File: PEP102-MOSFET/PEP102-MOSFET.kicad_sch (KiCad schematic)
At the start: 23 parts, among them J1 Screw_Terminal_01x02, J2 Screw_Terminal_01x02, J3 Screw_Terminal_01x02, J4 Screw_Terminal_01x02, J5 Screw_Terminal_01x02, Q13 AO3400A, Q8 AO3401A

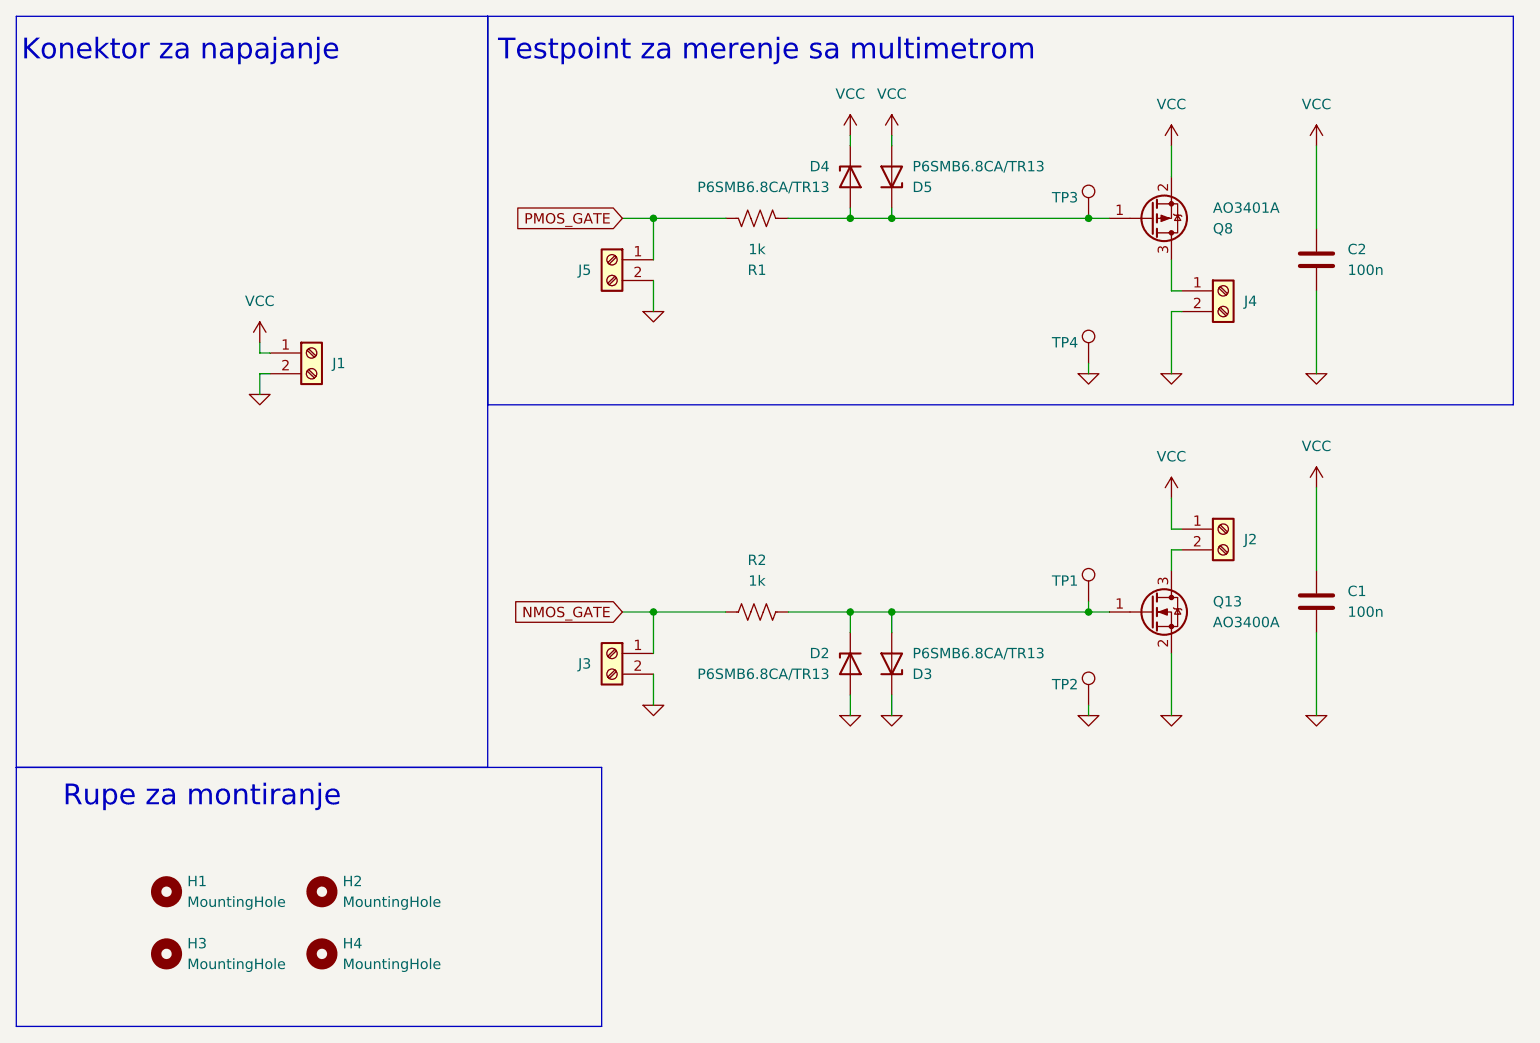
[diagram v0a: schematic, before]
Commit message: Uklonjen PMOS sa PEP102 jer nema prostora.
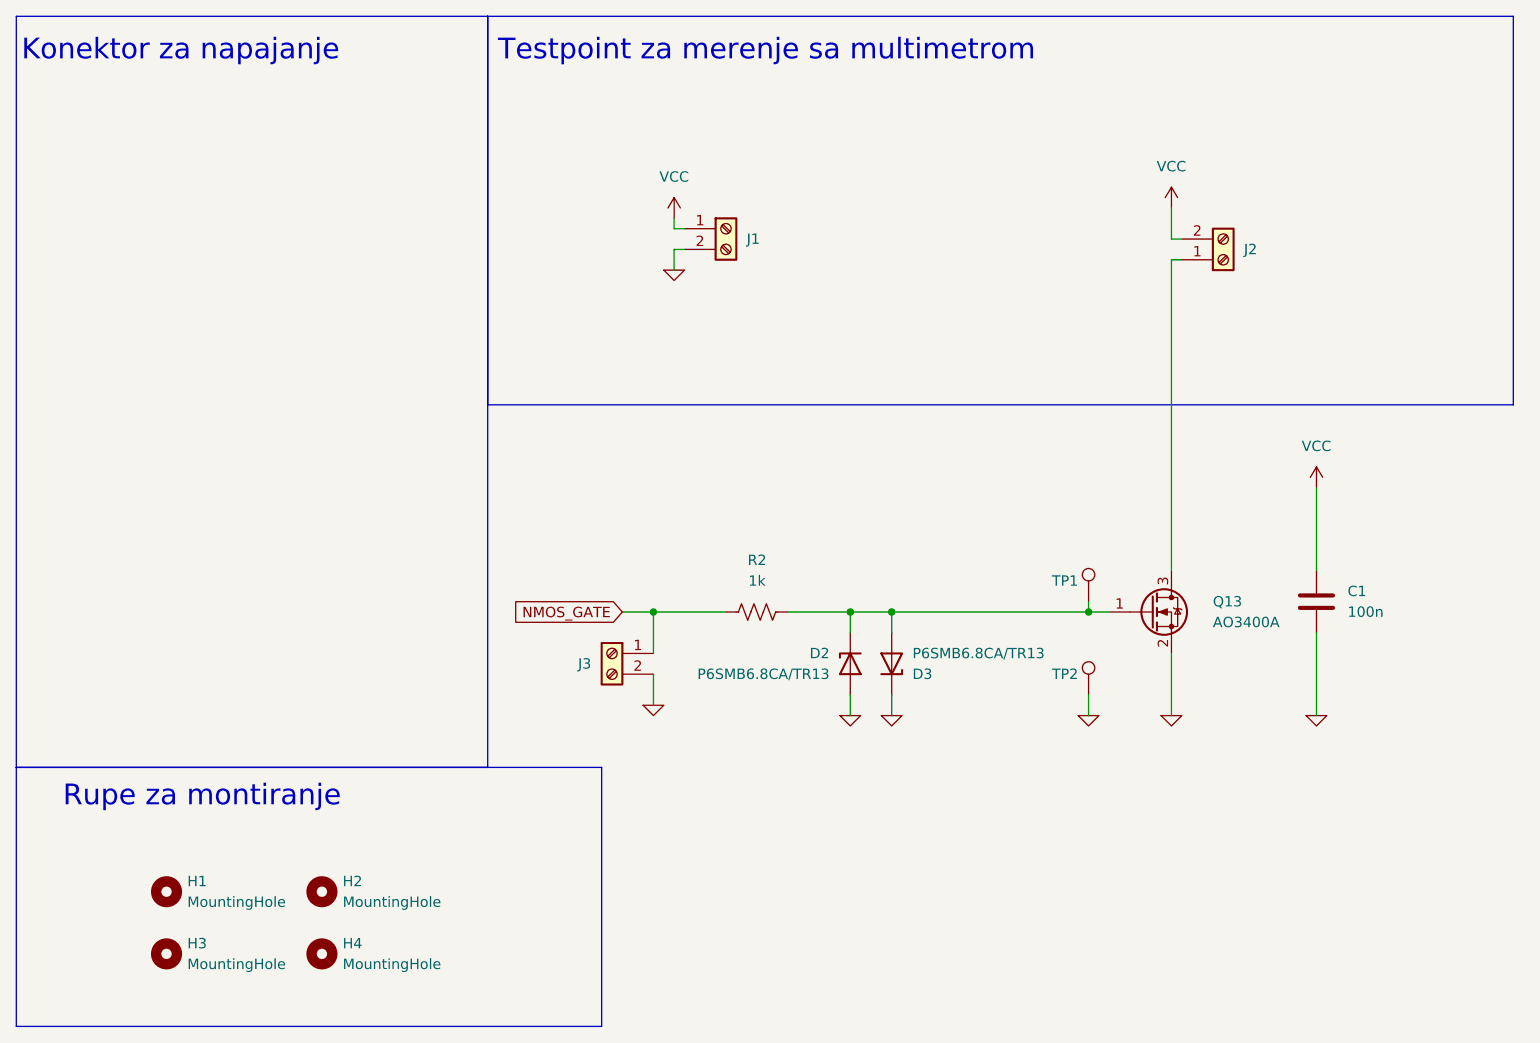
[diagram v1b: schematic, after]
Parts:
- removed C2: 100n, Capacitor_SMD:C_1206_3216Metric_Pad1.33x1.80mm_HandSolder, symbol Device:C
- removed D4, D5: P6SMB6.8CA/TR13, Diode_SMD:D_SMB_Handsoldering, symbol Device:D_Zener
- removed J4, J5: Screw_Terminal_01x02, PEP_library:TerminalBlock_Phoenix_MKDS-1,5-2-5.08_1x02_P5.08mm_Horizontal, symbol PEP_library:Screw_Terminal_01x02
- removed Q8: AO3401A, Package_TO_SOT_SMD:SOT-23, symbol Transistor_FET:AO3401A
- removed R1: 1k, Resistor_SMD:R_1206_3216Metric_Pad1.30x1.75mm_HandSolder, symbol Device:R_US
- removed TP3, TP4: TestPoint, symbol Connector:TestPoint
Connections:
- net VCC: now also J2.2 (Pin_2); no longer J2.1 (Pin_1)
- net at Q13.3 (D): now also J2.1 (Pin_1); no longer J2.2 (Pin_2)
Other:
- moved on the sheet: J1, J2, TP2

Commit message: Placement done.
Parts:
- removed D2, D3: P6SMB6.8CA/TR13, Diode_SMD:D_SMB_Handsoldering, symbol Device:D_Zener
- removed Q13: AO3400A, Package_TO_SOT_SMD:SOT-23, symbol Transistor_FET:AO3400A
- added D14: PSM712-LF-T7, Package_TO_SOT_SMD:SOT-23, symbol Device:D_Zener_Dual_CommonAnode_KKA
- added Q19: 2N7002, Package_TO_SOT_SMD:SOT-23, symbol Transistor_FET:AO3400A
- added TP3: TestPoint, TestPoint:TestPoint_Pad_D4.0mm, symbol Connector:TestPoint
- TP1, TP2: footprint (none) -> TestPoint:TestPoint_Pad_D4.0mm
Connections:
- net 0: now also D14.3 (A), Q19.2 (S)
- net VCC: now also J2.1 (Pin_1); no longer J2.2 (Pin_2)
- net at R2.2, TP1.1: now also D14.1 (K), D14.2 (K), Q19.1 (G)
- new net: J2.2 (Pin_2), Q19.3 (D), TP3.1

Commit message: Done, kinda
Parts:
- J2: footprint PEP_library:TerminalBlock_Phoenix_MKDS-1,5-2-5.08_1x02_P5.08mm_Horizontal -> PEP_library:Screw terminal
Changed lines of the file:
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@@
 			)
 		)
-		(property "Footprint" "PEP_library:TerminalBlock_Phoenix_MKDS-1,5-2-5.08_1x02_P5.08mm_Horizontal"
+		(property "Footprint" "PEP_library:Screw terminal"
 			(at 160.02 39.37 0)
 			(effects

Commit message: Done, kinda
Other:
- note added: "MOSFET"
- note added: "Zaštita gate-a"
- note removed: "Testpoint za merenje sa multimetrom"
- moved on the sheet: C1, D14, J1, J2, J3, Q19, R2, TP1, TP2, TP3

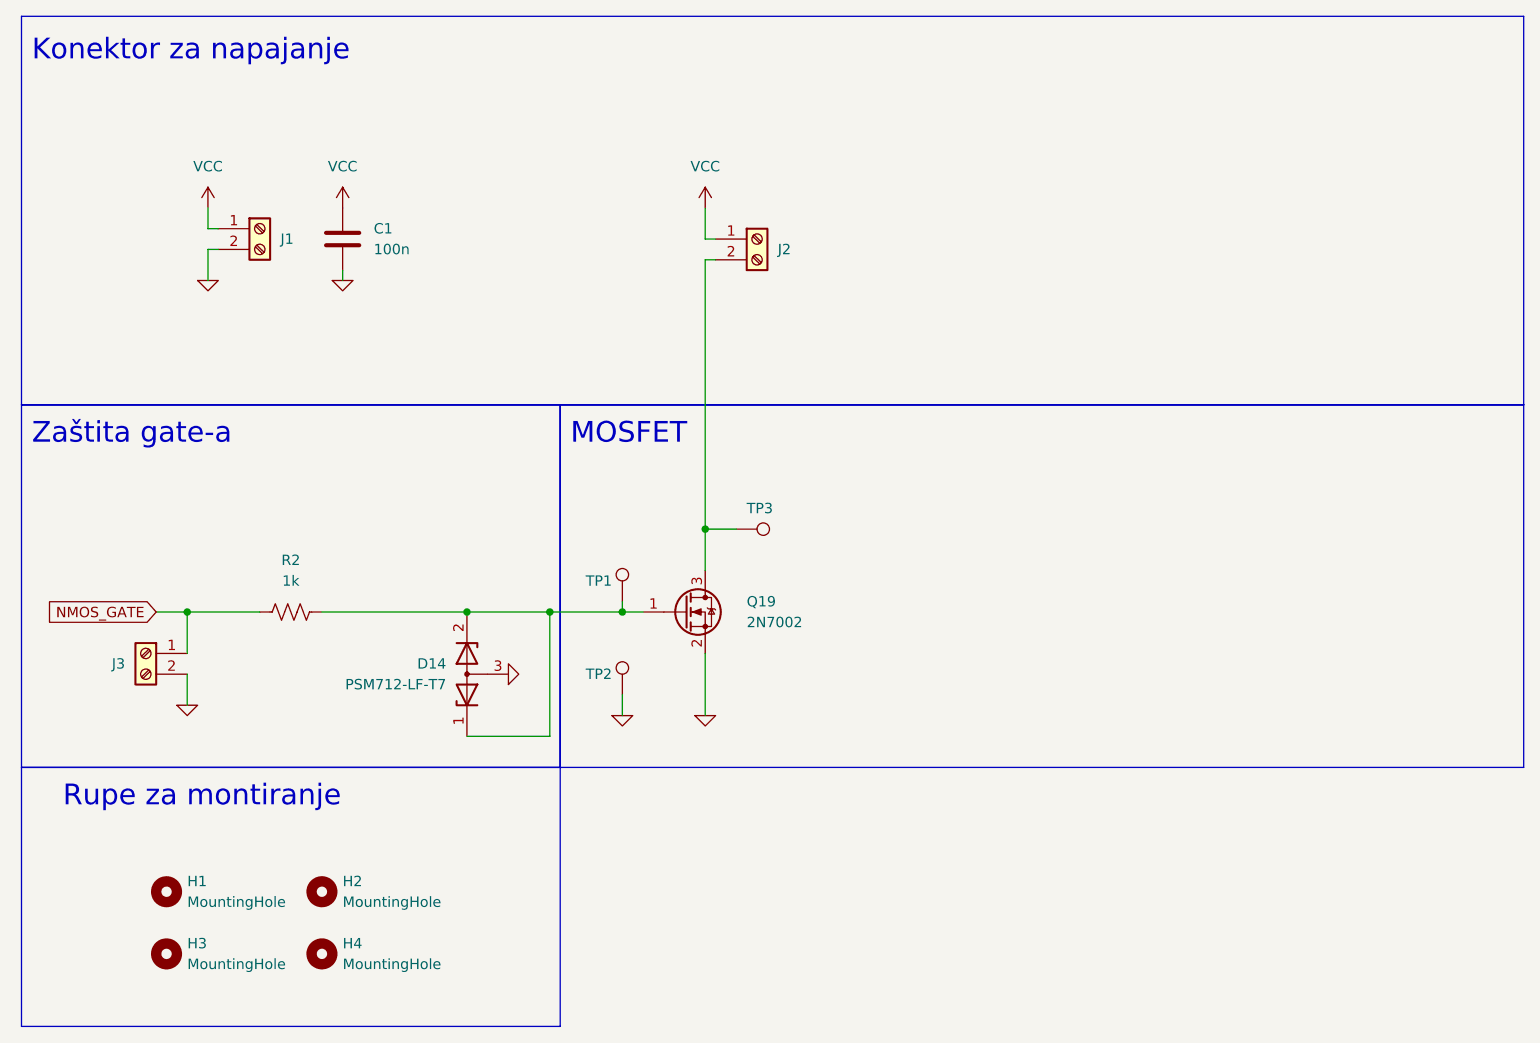
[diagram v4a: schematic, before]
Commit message: MOSFET updated.
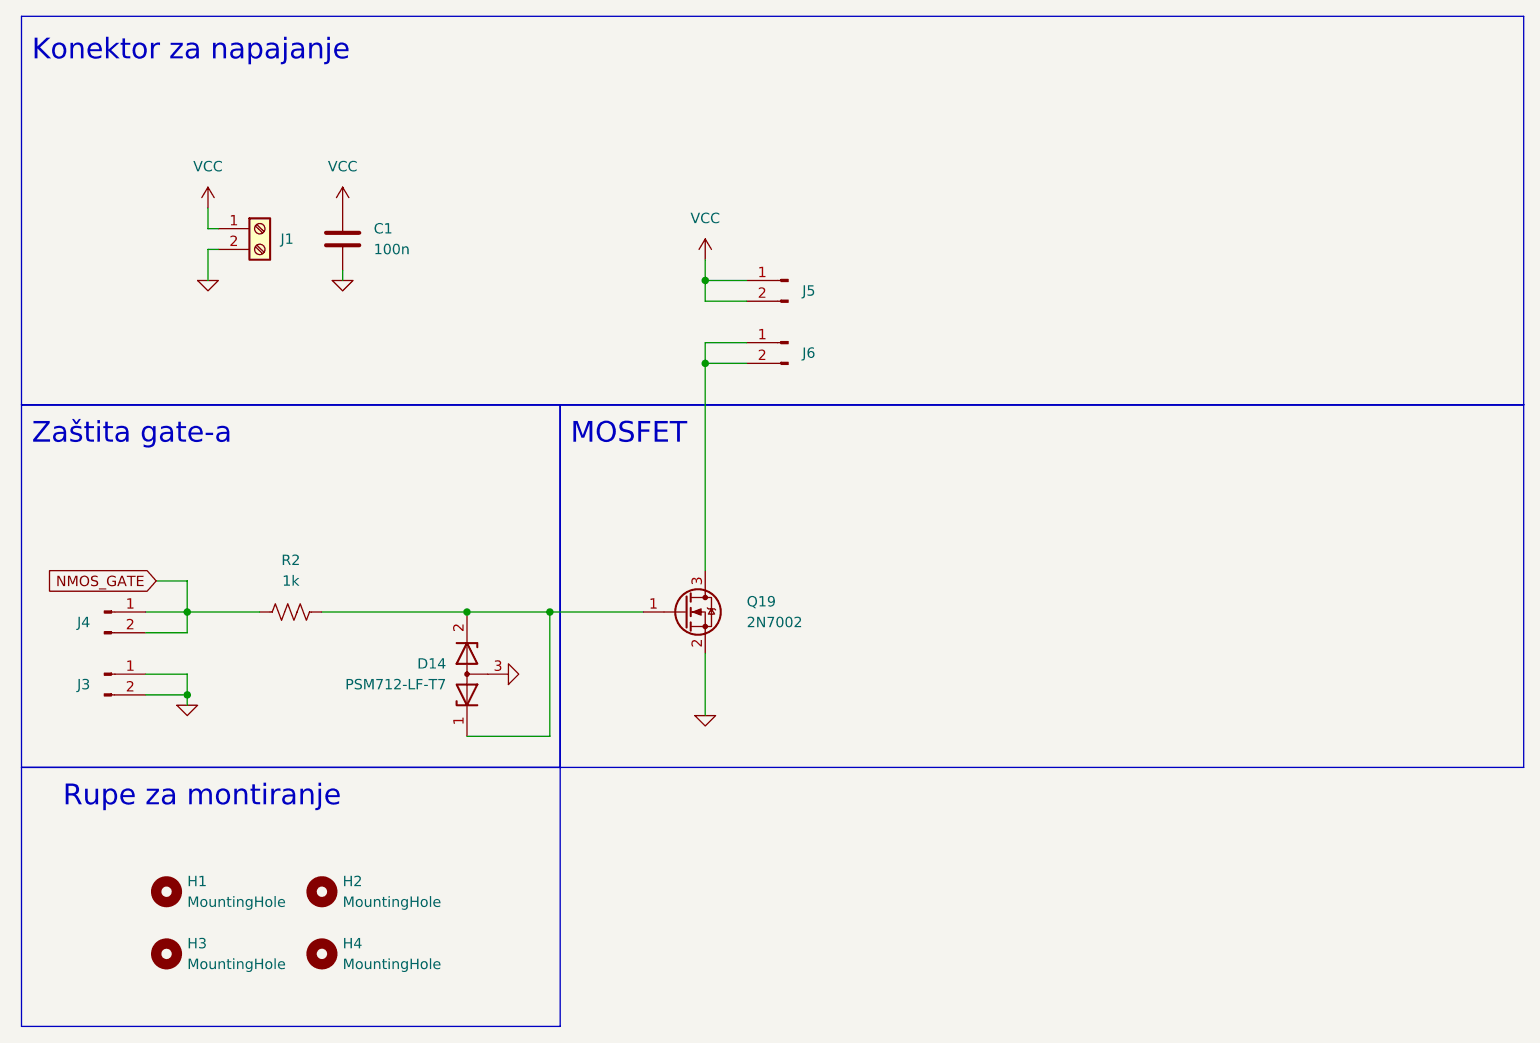
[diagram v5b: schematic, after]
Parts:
- removed J2: Screw_Terminal_01x02, PEP_library:Screw terminal, symbol PEP_library:Screw_Terminal_01x02
- removed J3: Screw_Terminal_01x02, PEP_library:TerminalBlock_Phoenix_MKDS-1,5-2-5.08_1x02_P5.08mm_Horizontal, symbol PEP_library:Screw_Terminal_01x02
- removed TP1, TP2, TP3: TestPoint, TestPoint:TestPoint_Pad_D4.0mm, symbol Connector:TestPoint
- added J3, J4, J5, J6: Conn_01x02_Pin, Connector_PinHeader_2.54mm:PinHeader_2x01_P2.54mm_Vertical, symbol Connector:Conn_01x02_Pin
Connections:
- net 0: now also J3.1 (Pin_1), J3.2 (Pin_2)
- net NMOS_GATE: now also J4.1 (Pin_1), J4.2 (Pin_2)
- net VCC: now also J5.1 (Pin_1), J5.2 (Pin_2)
- net at Q19.3 (D): now also J6.1 (Pin_1), J6.2 (Pin_2)
